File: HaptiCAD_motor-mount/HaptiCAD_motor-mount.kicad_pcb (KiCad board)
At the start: 4 copper layers, 170 x 110 mm, 15 parts, among them U401 MT6701CT, U501 AP2112K-3.3

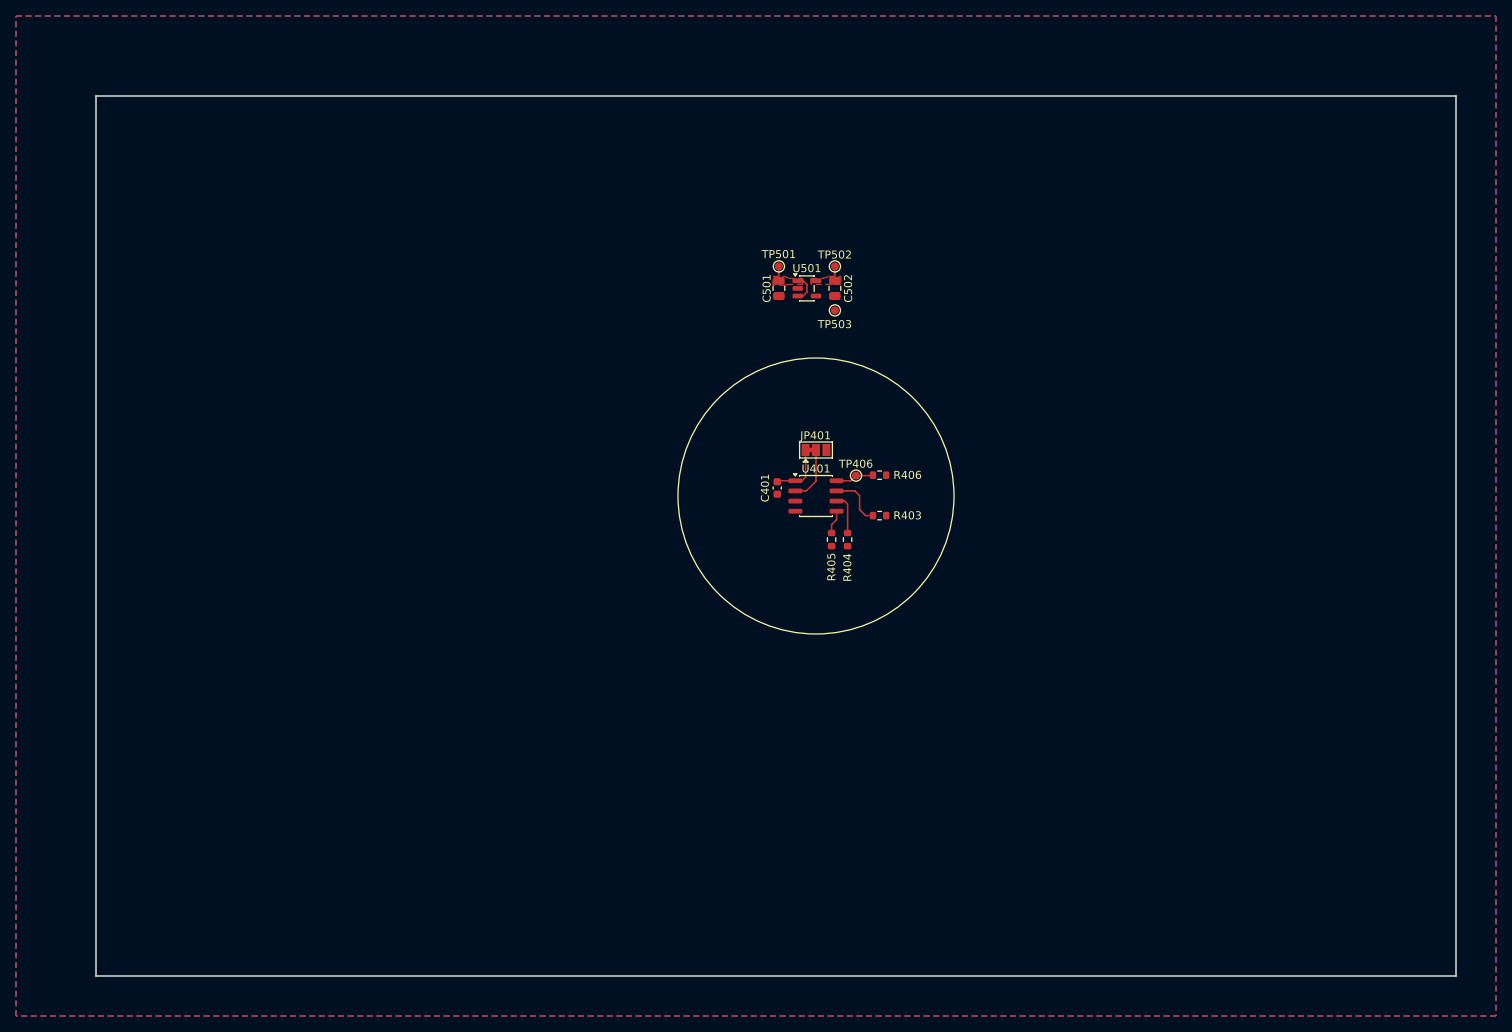
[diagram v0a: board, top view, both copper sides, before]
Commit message: Finished the layout for the base and motor mount
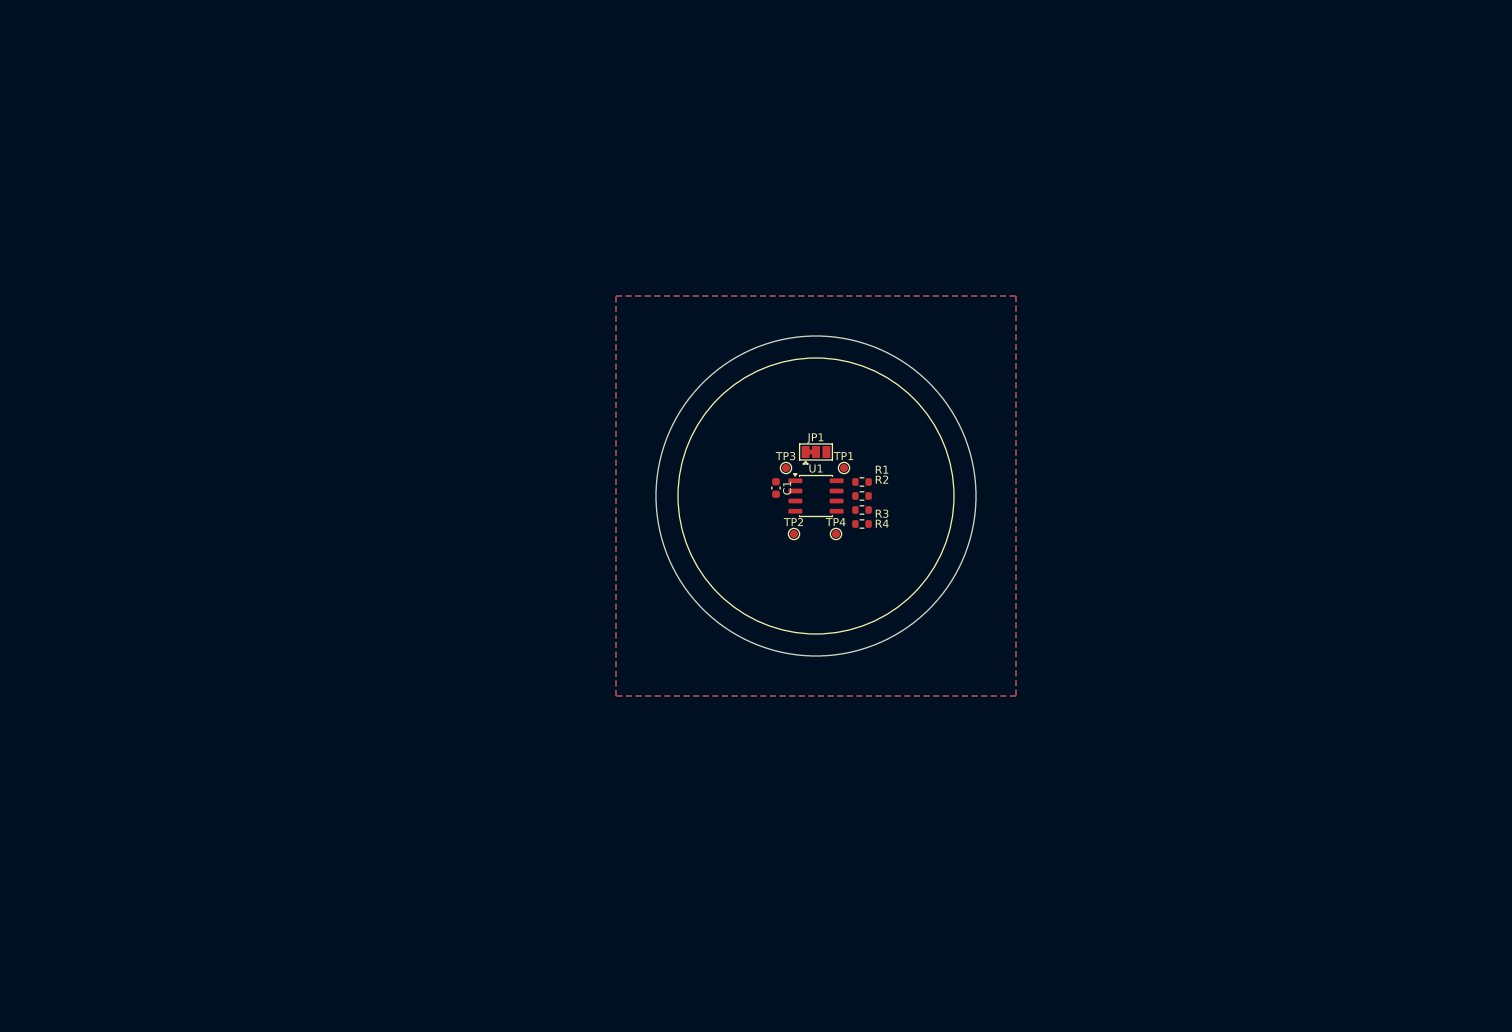
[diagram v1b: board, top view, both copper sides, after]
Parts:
- removed C401: 0.1uF, Capacitor_SMD:C_0603_1608Metric
- removed C501, C502: 10uF, Capacitor_SMD:C_0805_2012Metric
- removed JP401: SolderJumper_3_Bridged12, Jumper:SolderJumper-3_P1.3mm_Bridged12_Pad1.0x1.5mm
- removed R403, R404: 2.2k, Resistor_SMD:R_0603_1608Metric
- removed R405: 100k, Resistor_SMD:R_0603_1608Metric
- removed R406: 0, Resistor_SMD:R_0603_1608Metric
- removed TP406: ENC__~{CS}, TestPoint:TestPoint_Pad_D1.0mm
- removed TP501: 5V, TestPoint:TestPoint_Pad_D1.0mm
- removed TP502: 3.3V, TestPoint:TestPoint_Pad_D1.0mm
- removed TP503: GND, TestPoint:TestPoint_Pad_D1.0mm
- removed U401: MT6701CT, Package_SO:SO-8_3.9x4.9mm_P1.27mm
- removed U501: AP2112K-3.3, Package_TO_SOT_SMD:SOT-23-5
- added C1: 0.1uF, Capacitor_SMD:C_0603_1608Metric, F.Cu at (135.0, 99.0)
- added JP1: SolderJumper_3_Bridged12, Jumper:SolderJumper-3_P1.3mm_Bridged12_Pad1.0x1.5mm, F.Cu at (140.0, 94.5)
- added R1: 0, Resistor_SMD:R_0603_1608Metric, F.Cu at (145.8, 98.2)
- added R2: 2.2k, Resistor_SMD:R_0603_1608Metric, F.Cu at (145.8, 100.0)
- added R3: 2.2k, Resistor_SMD:R_0603_1608Metric, F.Cu at (145.8, 101.8)
- added R4: 100k, Resistor_SMD:R_0603_1608Metric, F.Cu at (145.8, 103.5)
- added TP1: ENC__~{CS}, TestPoint:TestPoint_Pad_D1.0mm, F.Cu at (143.5, 96.5)
- added TP2: GND, TestPoint:TestPoint_Pad_D1.0mm, F.Cu at (137.2, 104.8)
- added TP3: 5V, TestPoint:TestPoint_Pad_D1.0mm, F.Cu at (136.2, 96.5)
- added TP4: 3.3V, TestPoint:TestPoint_Pad_D1.0mm, F.Cu at (142.5, 104.8)
- added U1: MT6701CT, Package_SO:SO-8_3.9x4.9mm_P1.27mm, F.Cu at (140.0, 100.0)
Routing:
- net 5V: track 12.6 -> 0.00 mm
- net Net-(JP401-C): track 6.98 -> 0.00 mm
- net /Sensors/ENC_CLK: track 6.85 -> 0.00 mm
- net /Sensors/ENC_MISO: track 5.14 -> 0.00 mm
- net /Sensors/ENC__~{CS}: track 4.89 -> 0.00 mm
- net /Sensors/ENC__PUSH: track 2.98 -> 0.00 mm
- net 3.3V: track 1.80 -> 0.00 mm
- removed copper zone on F.Cu, net 3.3V
- removed copper zone on F.Cu, net 5V
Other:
- board size 170 x 110 mm -> 40 x 40 mm
